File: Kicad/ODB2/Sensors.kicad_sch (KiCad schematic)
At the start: 0 parts

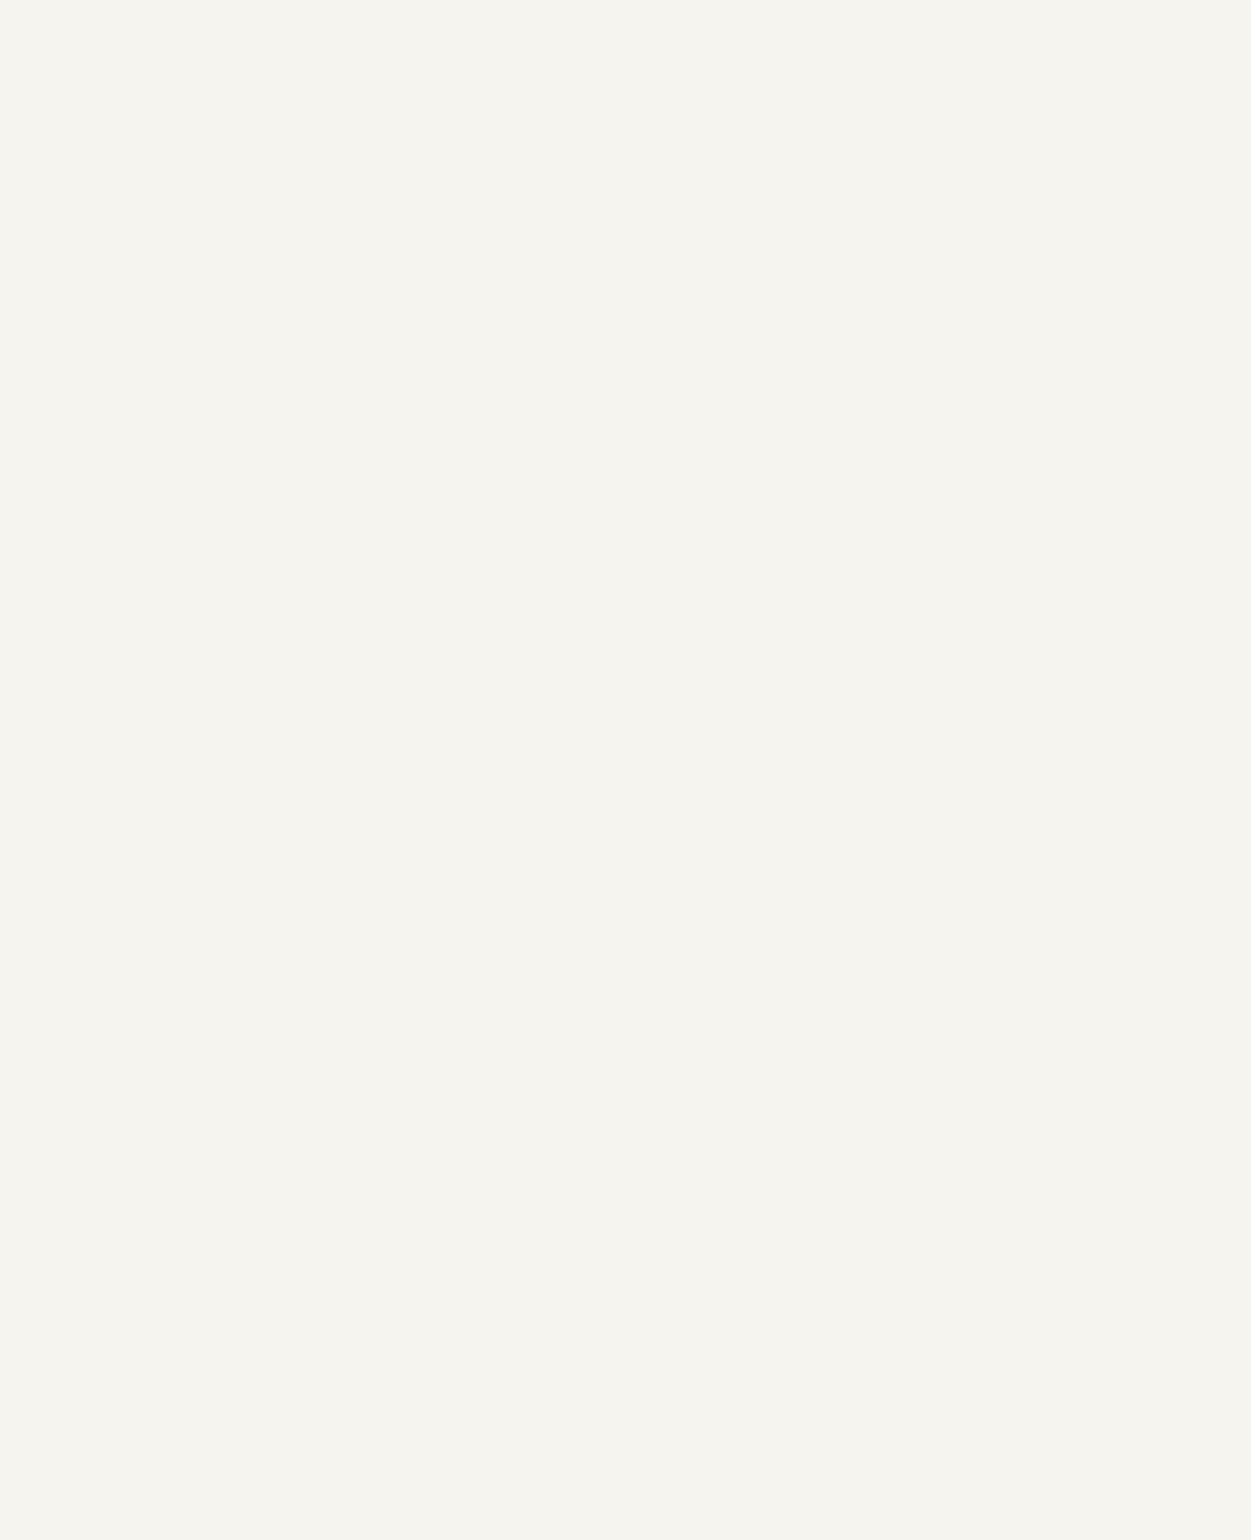
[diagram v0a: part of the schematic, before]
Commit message: add pages specific component
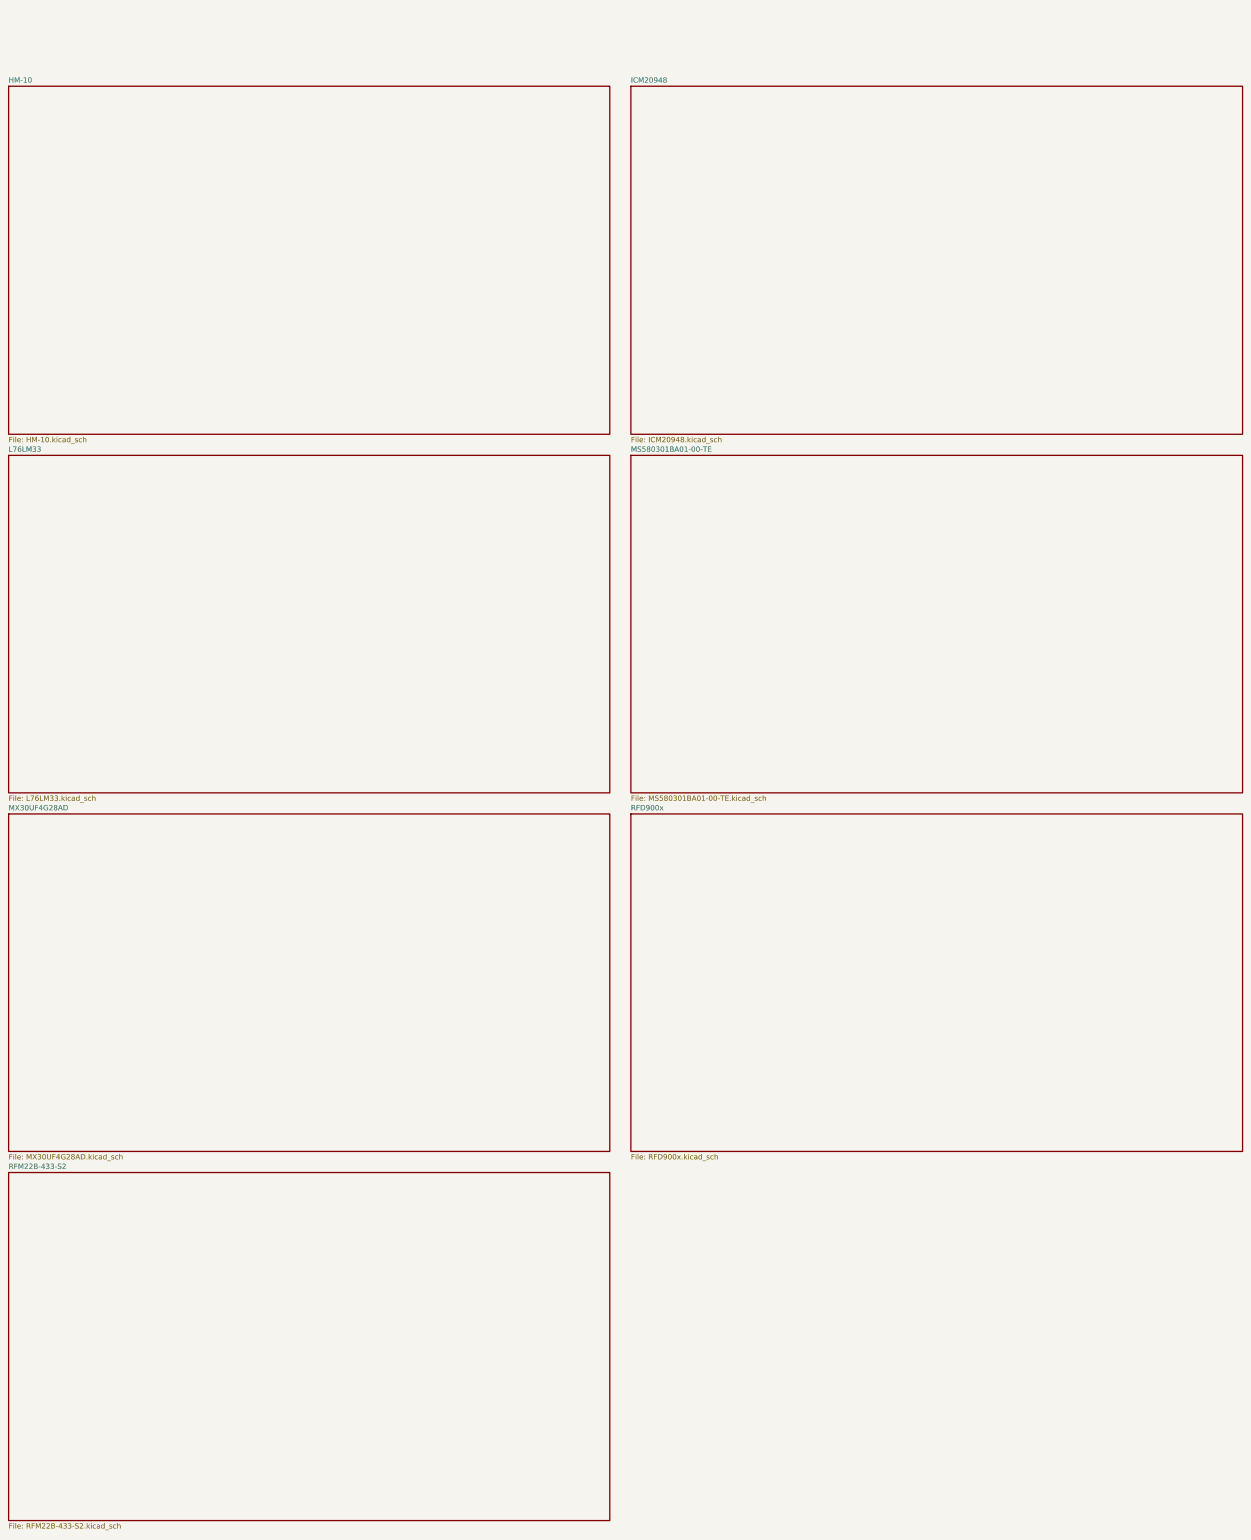
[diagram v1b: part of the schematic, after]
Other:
- added sheet HM-10 (HM-10.kicad_sch)
- added sheet ICM20948 (ICM20948.kicad_sch)
- added sheet L76LM33 (L76LM33.kicad_sch)
- added sheet MS580301BA01-00-TE (MS580301BA01-00-TE.kicad_sch)
- added sheet MX30UF4G28AD (MX30UF4G28AD.kicad_sch)
- added sheet RFD900x (RFD900x.kicad_sch)
- added sheet RFM22B-433-S2 (RFM22B-433-S2.kicad_sch)

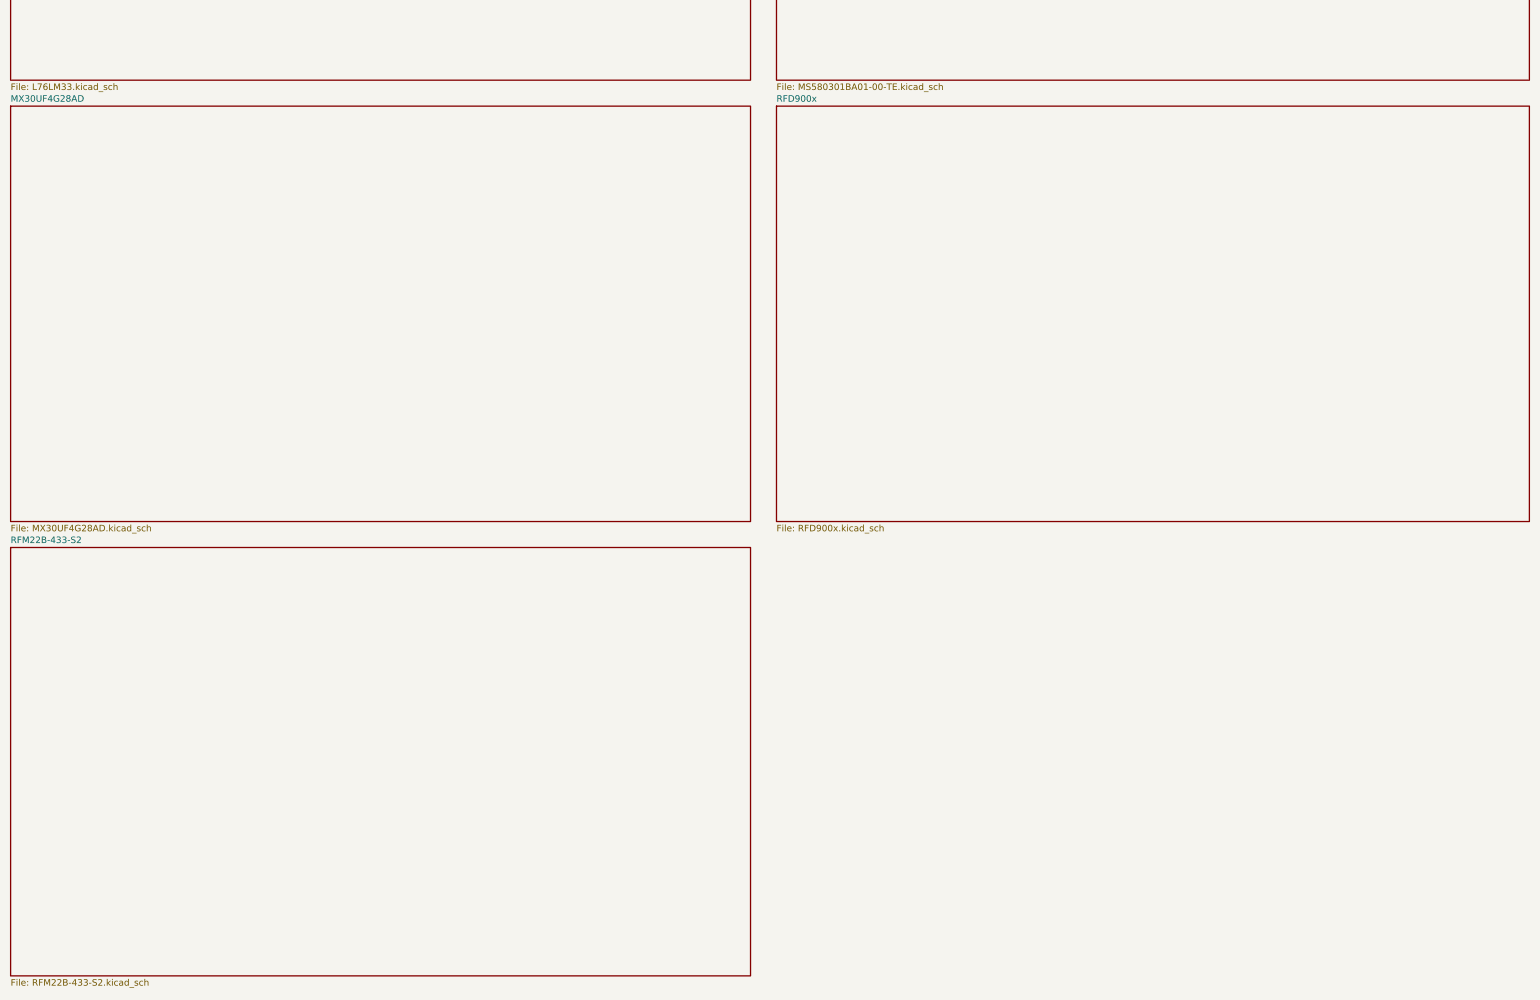
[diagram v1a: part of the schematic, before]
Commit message: add C decoupling
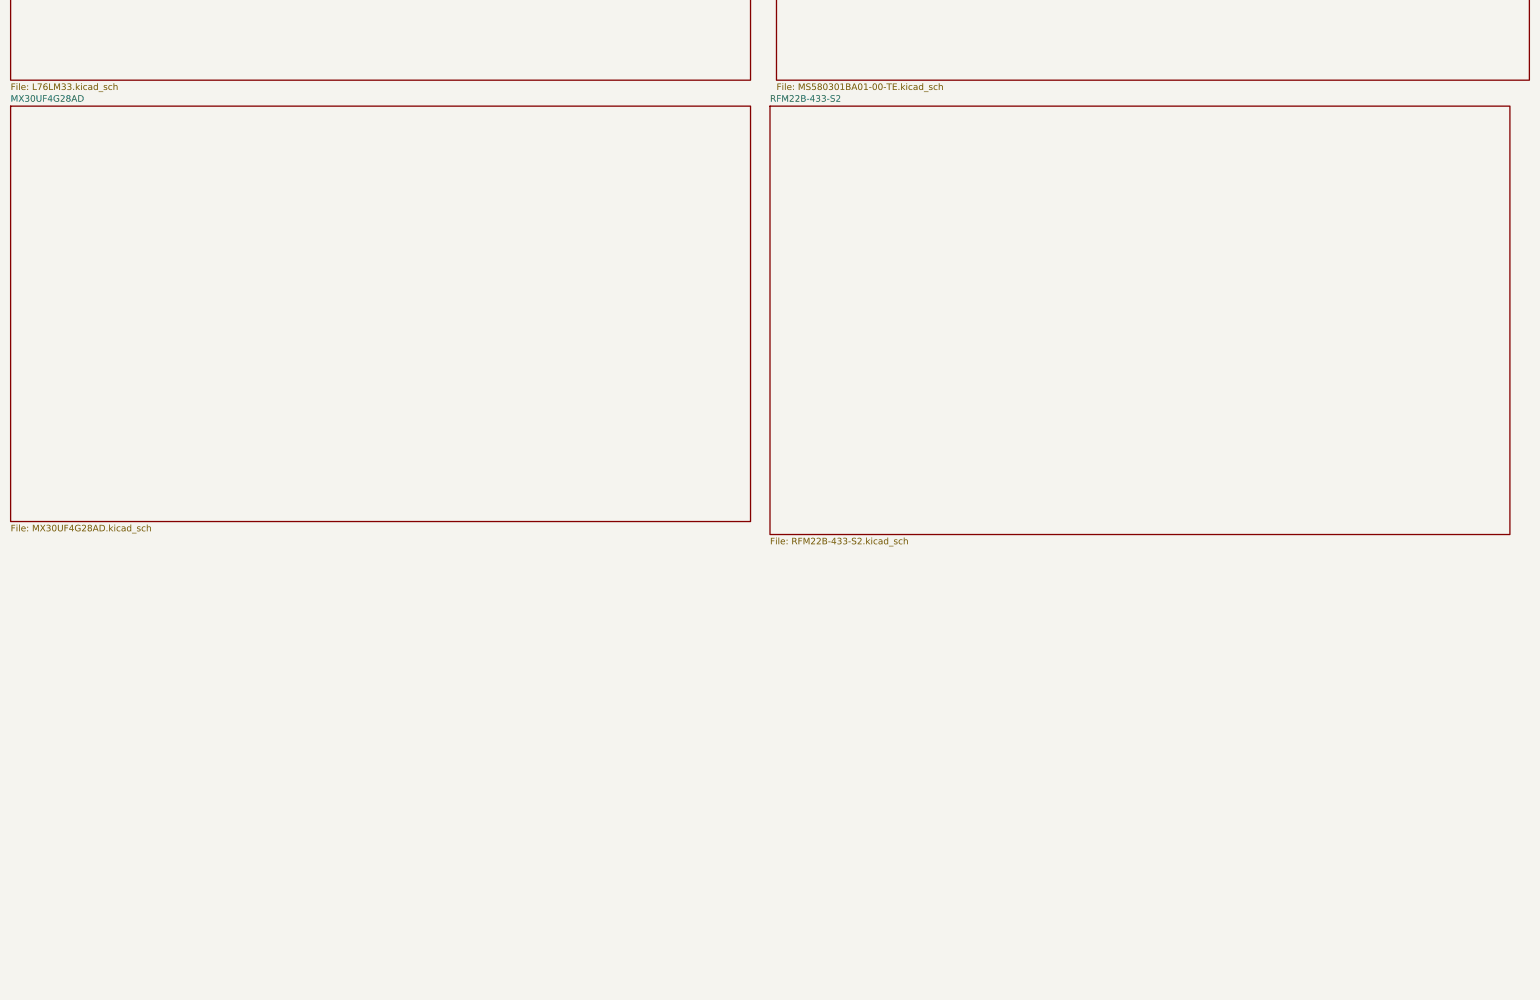
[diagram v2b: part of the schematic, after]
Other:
- removed sheet RFD900x
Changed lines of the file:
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@@
 	)
 	(sheet
-		(at 0 474.98)
+		(at 148.59 388.62)
 		(size 144.78 83.82)
 		(fields_autoplaced yes)
@@
 		)
 		(property "Sheetname" "RFM22B-433-S2"
-			(at 0 474.2684 0)
+			(at 148.59 387.9084 0)
 			(effects
 				(font
@@
 		)
 		(property "Sheetfile" "RFM22B-433-S2.kicad_sch"
-			(at 0 559.3846 0)
+			(at 148.59 473.0246 0)
 			(effects
 				(font
@@
 				)
 			)
-		)
-	)
-	(sheet
-		(at 149.86 388.62)
-		(size 147.32 81.28)
-		(fields_autoplaced yes)
-		(stroke
-			(width 0.1524)
-			(type solid)
-		)
-		(fill
-			(color 0 0 0 0.0000)
-		)
-		(property "Sheetname" "RFD900x"
-			(at 149.86 387.9084 0)
-			(effects
-				(font
-					(size 1.27 1.27)
-				)
-				(justify left bottom)
-			)
-		)
-		(property "Sheetfile" "RFD900x.kicad_sch"
-			(at 149.86 470.4846 0)
-			(effects
-				(font
-					(size 1.27 1.27)
-				)
-				(justify left top)
-			)
-		)
-		(instances
-			(project "ODB2"
-				(path "/4b06c5d1-aa8b-48ed-8972-b43a60cfab78/eac5f07f-d6a3-4c95-b286-7cebf46e30db"
-					(page "11")
-				)
-			)

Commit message: merge all sensors to main page + fix NC
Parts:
- added BT_C1: 10uF, symbol Device:C
- added BT_C2, Baro_C1, ICM_C1, ICM_C2: 100nF, symbol Device:C
- added BT_R1: 10k, symbol Device:R
- added BT_R2, BT_R3: 1k5, Resistor_SMD:R_0805_2012Metric, symbol Device:R
- added E1: HM-10, HM-10:26.9X13X2.2_BOARD, symbol ODB_Lib:HM-10
- added GPS_C1: 100nf, symbol Device:C
- added GPS_L1: 100nH, Inductor_SMD:L_0805_2012Metric, symbol Device:L
- added GPS_R1: 10R, Resistor_SMD:R_0805_2012Metric, symbol Device:R
- added J4: RF2-04A-T-00-50-G, Connector_Coaxial:SMA_Wurth_60312002114503_Vertical, symbol Connector:Conn_Coaxial
- added J5: RFM_Conn_Coaxial, symbol Connector:Conn_Coaxial
- added LED_BT1: BT_LED1_G, LED_SMD:LED_0805_2012Metric, symbol Device:LED
- added U5: L76L-M33, L76_QWS, symbol ODB_Lib:L76L-M33
- added U6: ICM-20948, QFN24_3X3X0P9_IVS, symbol ODB_Lib:ICM-20948
- added U7: MS580301BA01-00, MS5803-01BA01_TEC, symbol ODB_Lib:MS580301BA01-00
- added U9: RFM23BP-433-S2, RFM23BP-433-S2:MODULE_RFM23BP-433-S2, symbol ODB2:RFM23BP-433-S2
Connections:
- new net: BT_R2.2, LED_BT1.2 (A)
- new net: BT_C2.1, BT_R1.1, E1.11 (RESET)
- new net: BT_R2.1, E1.24 (LED)
- new net: GPS_L1.1, GPS_R1.1
- new net: GPS_R1.2, U5.14 (VCC_REF)
- new net: ICM_C1.1, U6.10 (REGOUT)
- new net +1V8: ICM_C2.1, U6.13 (VDD), U6.8 (VDDIO)
- new net +3V3: BT_C1.1, BT_R1.2, BT_R3.2, Baro_C1.2, E1.12 (+3.3V), GPS_C1.2, U5.6 (V_BCKP), U5.8 (VCC), U5.9 (RESET), U7.1 (VDD), U9.5 (VCC)
- new net GND: BT_C1.2, BT_C2.2, BT_R3.1, Baro_C1.1, E1.13 (GND), E1.14 (GND__1), E1.21 (GND__2), E1.22 (GND__3), E1.23 (KEY), GPS_C1.1, ICM_C1.2, ICM_C2.2, J4.2 (Ext), J5.2 (Ext), LED_BT1.1 (K), U5.1 (GND), U5.10 (GND), U5.12 (GND), U6.11 (FSYNC), U6.18 (GND), U6.20 (RESV_GND), U7.2 (PS), U7.3 (GND), U9.16 (GND__1), U9.2 (GND__2)
- new net GPS_RF: GPS_L1.2, J4.1 (In), U5.11 (RF_IN)
- new net ICM_INT: U6.12 (INT1)
- new net RFM_ANT: J5.1 (In), U9.1 (ANT)
- new net RFM_NIRQ: U9.14 (NIRQ)
- new net RFM_SDN: U9.15 (SDN)
- new net SPI1_ICM_CS: U6.22 (nCS)
- new net SPI1_ICM_MISO: U6.9 (SDO/AD0)
- new net SPI1_ICM_MOSI: U6.24 (SDA/SDI)
- new net SPI1_ICM_SCLK: U6.23 (SCL/SCLK)
- new net SPI2_RFM_CS: U9.13 (NSEL)
- new net SPI2_RFM_MISO: U9.10 (SDO)
- new net SPI2_RFM_MOSI: U9.11 (SDI)
- new net SPI2_RFM_SCK: U9.12 (SCK)
- new net UART1_GPS_RX: U5.3 (RXD1)
- new net UART1_GPS_TX: U5.2 (TXD1)
- new net UART2_BT_RX: E1.1 (UART_TX)
- new net UART2_BT_TX: E1.2 (UART_RX)
- no-connect marks 0 -> 37
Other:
- removed sheet HM-10
- removed sheet ICM20948
- removed sheet L76LM33
- removed sheet MS580301BA01-00-TE
- removed sheet MX30UF4G28AD
- removed sheet RFM22B-433-S2
- note added: "Accelerometer"
- note added: "Barometer"
- note added: "Beacon"
- note added: "Bluetooth"
- note added: "GPS"
- note added: "Intégration pour antenne active"
- note added: "Memory"

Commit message: Footprints des sensors
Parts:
- E1: footprint HM-10:26.9X13X2.2_BOARD -> ODB:HM-10
- U5: footprint L76_QWS -> ODB:L76_QWS
- U6: footprint QFN24_3X3X0P9_IVS -> ODB:ICM-L
- U7: footprint MS5803-01BA01_TEC -> ODB:MS5803-01BA01_TEC
- U9: footprint RFM23BP-433-S2:MODULE_RFM23BP-433-S2 -> ODB:RFM22B-433-S2
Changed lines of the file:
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@@
 			)
 		)
-		(property "Footprint" "HM-10:26.9X13X2.2_BOARD"
+		(property "Footprint" "ODB:HM-10"
 			(at 186.69 25.4 0)
 			(effects
@@
 			)
 		)
-		(property "Footprint" "QFN24_3X3X0P9_IVS"
+		(property "Footprint" "ODB:ICM-L"
 			(at 71.882 76.708 0)
 			(effects
@@
 			)
 		)
-		(property "Footprint" "RFM23BP-433-S2:MODULE_RFM23BP-433-S2"
+		(property "Footprint" "ODB:RFM22B-433-S2"
 			(at 60.96 171.45 0)
 			(effects
@@
 			)
 		)
-		(property "Footprint" "MS5803-01BA01_TEC"
+		(property "Footprint" "ODB:MS5803-01BA01_TEC"
 			(at 57.404 112.014 0)
 			(effects
@@
 			)
 		)
-		(property "Footprint" "L76_QWS"
+		(property "Footprint" "ODB:L76_QWS"
 			(at 67.818 37.846 0)
 			(effects
